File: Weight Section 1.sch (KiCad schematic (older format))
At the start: 43 parts, among them Q1 2SK3018, Q10 2SK3018, Q11 2SK3018, Q12 2SK3018, Q2 2SK3018, Q3 2SK3018, Q4 2SK3018, Q5 2SK3018, Q6 2SK3018, Q7 2SK3018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

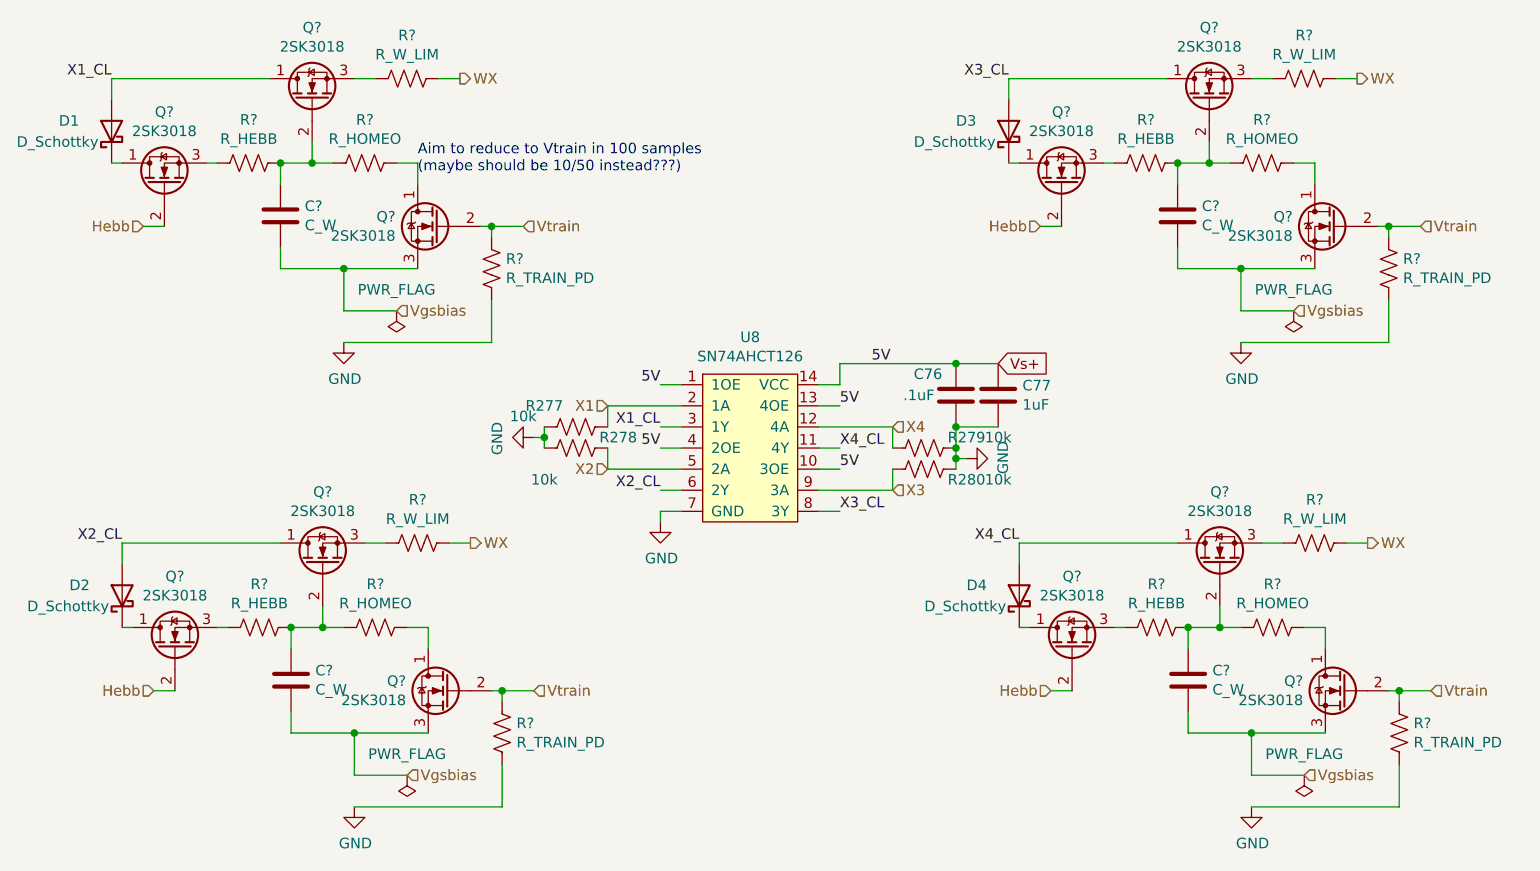
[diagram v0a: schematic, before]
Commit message: Likely Final Component Values
Most values for components that are not dependent on synapse number have been selected.
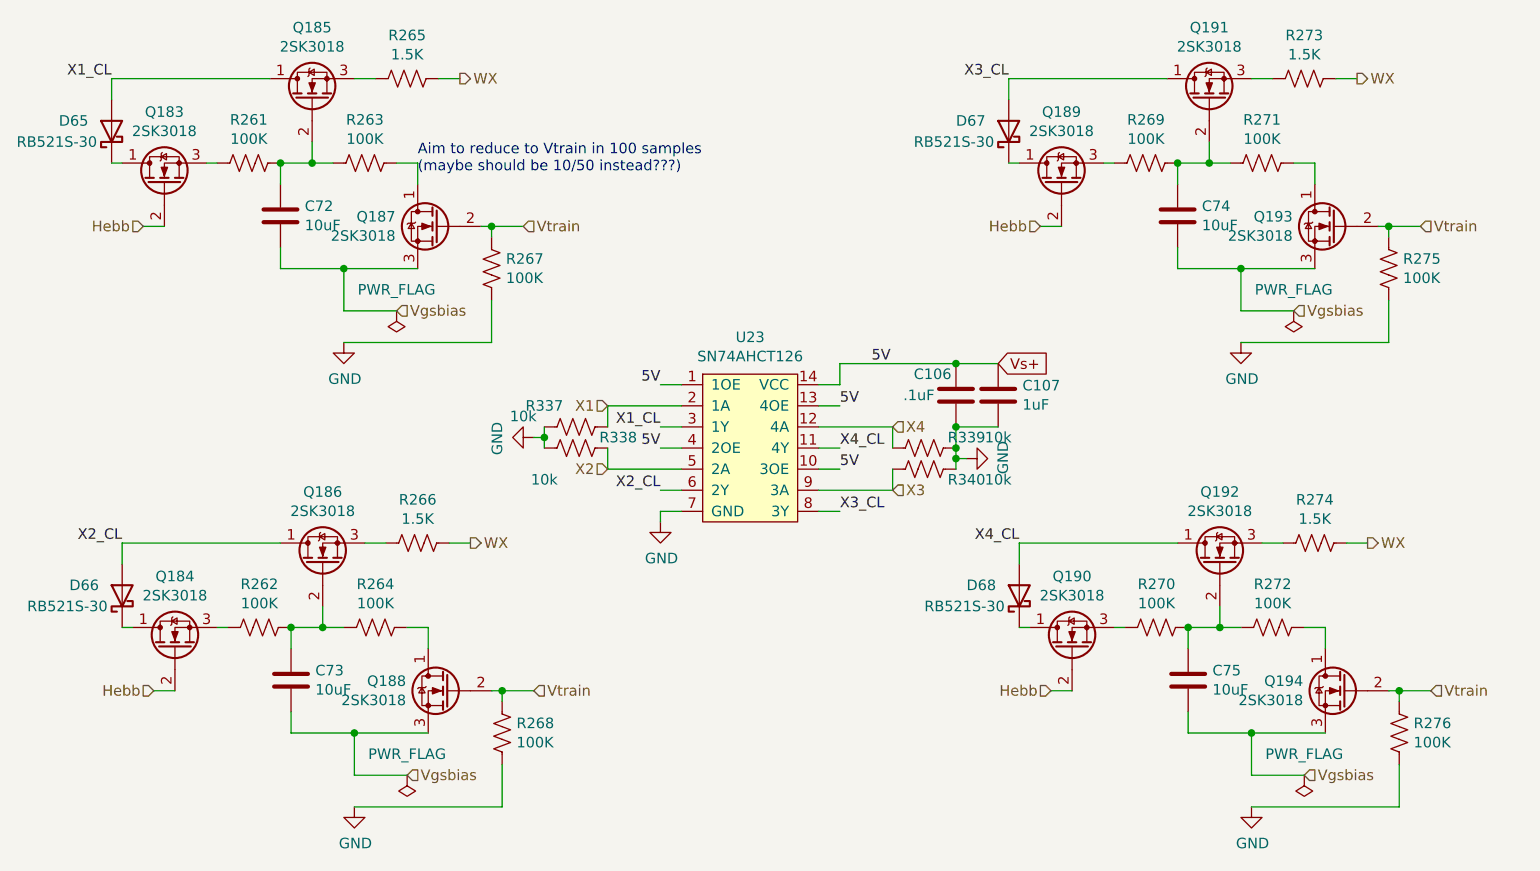
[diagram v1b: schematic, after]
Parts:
- C1, C2, C3, C4: value C_W -> 10uF
- D1, D2, D3, D4: value D_Schottky -> RB521S-30
- R1, R10, R2, R9: value R_HEBB -> 100K
- R11, R12, R3, R4: value R_HOMEO -> 100K
- R13, R14, R5, R6: value R_W_LIM -> 1.5K
- R15, R16, R7, R8: value R_TRAIN_PD -> 100K
